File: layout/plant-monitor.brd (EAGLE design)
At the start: 42.2 x 23.8 mm, 11 parts, among them J1 AVR_SPI_PRG_6PTH

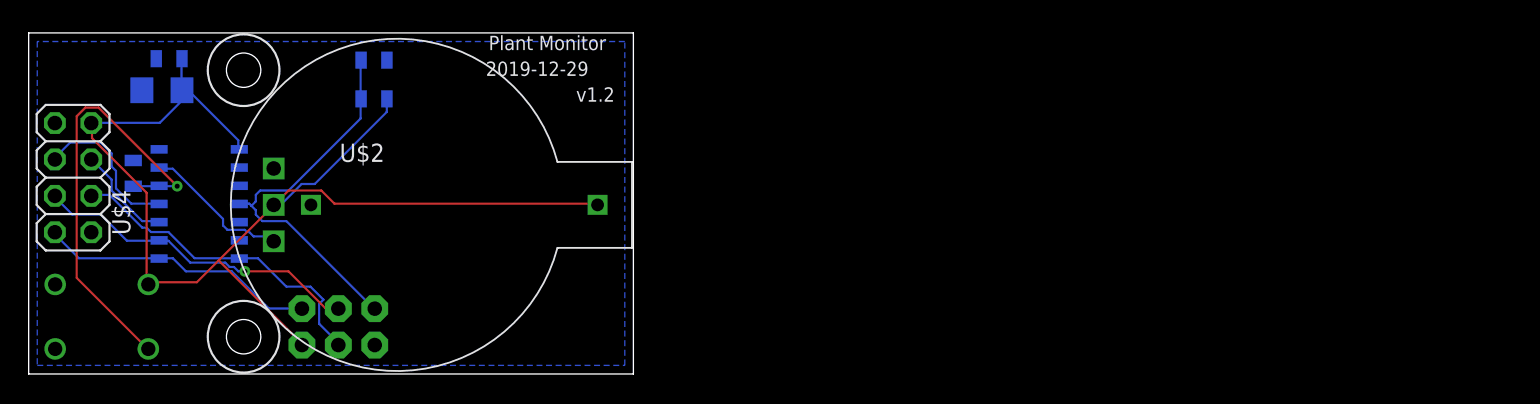
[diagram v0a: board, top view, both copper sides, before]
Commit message: Updated design to address problems in v1.3 board, notably ower switching added for soil sensor
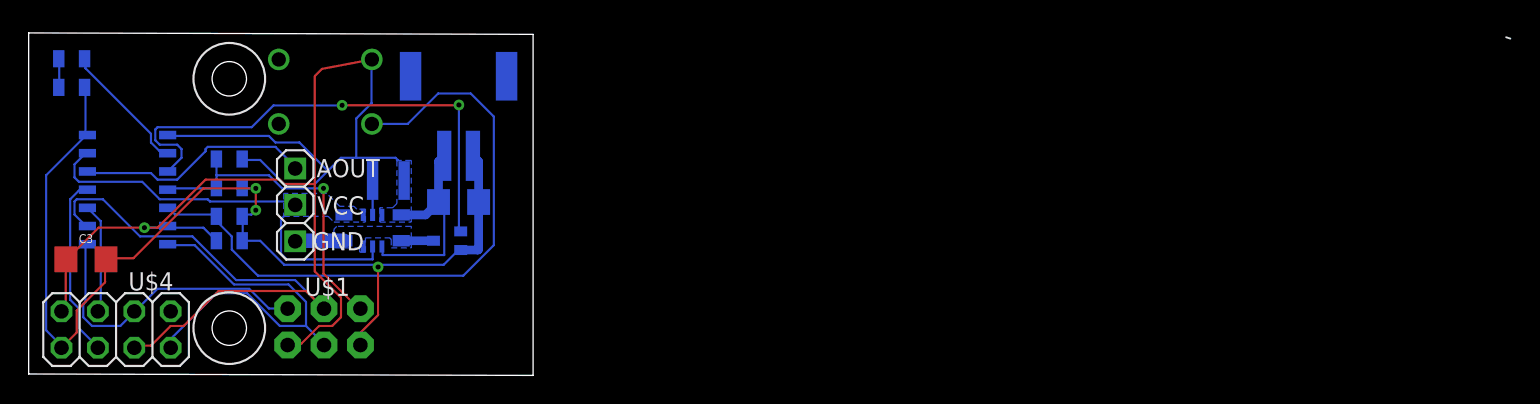
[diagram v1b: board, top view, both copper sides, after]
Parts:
- added C3: 10uF, SparkFun-Capacitors:1206
- added C5, C6: 10u, SparkFun:0805
- added R2: 300, SparkFun:0805
- added U$5: TPS6122X, GARTH:SC70-6
- added U$6: LED, GARTH:0805
- added U$8: BATT, GARTH:JST-PH-2
- added U$9: DMN53D0LW, GARTH:SOT-323
- U$1: value CAP-SOIL-SENSORRA -> CAP-SOIL-SENSOR; device GARTH:CAP-SOIL-SENSOR-RA -> GARTH:CAP-SOIL-SENSOR
- U$2: value 20MM-COIN-BATT -> 4.7u; device GARTH:20MM-COIN-BATT -> GARTH:LQH3NPN
- moved U$7 22.1 mm to (20.7, 19.7)
- moved C1 22.1 mm to (30.0, 12.0), turned to 180 degrees
- moved C4 13.5 mm to (14.0, 13.0)
- moved C2 13.4 mm to (14.0, 9.30), turned to 180 degrees
- moved U$4 11.0 mm to (6.10, 3.10), turned to 180 degrees
- moved R8 10.9 mm to (14.0, 15.0)
- moved R1 7.34 mm to (14.0, 11.0), turned to 0 degrees
- moved U$2 5.66 mm to (25.1, 13.5), flipped to the bottom
- moved U$3 5.10 mm to (6.90, 13.5)
- moved U$1 1.50 mm to (18.6, 11.8), flipped to the top, turned to 90 degrees
- moved J1 1.00 mm to (18.1, 4.56)
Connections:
- removed net MISO-DO: J1.1, U$3.8, U$4.MISO
- removed net MOSI-DI: J1.4, U$3.7, U$4.MOSI
- new net DI/(SPI-MOSI): J1.4, U$3.7, U$4.MISO
- new net DO/(SPI-MISO): J1.1, U$3.8, U$4.MOSI
- new net INDICATOR: R2.2, U$3.2
- new net N$1: R2.1, U$6.P$1
- new net N$2: U$2.P$2, U$5.P$5
- new net N$5: C5.2, C6.2, U$1.GND, U$5.P$3, U$9.P$1
- new net SENSOR_EN: U$3.3, U$9.P$2
- new net V5: C5.1, U$1.VCC, U$3.13, U$5.P$2, U$5.P$4
- net GND: now also C3.2, U$6.P$2, U$8.P$2, U$9.P$3; no longer U$1.GND, U$2.V-
- net SENSOR: now also U$3.12; no longer U$3.13
- net SETUP: now also U$3.5; no longer U$3.12
- net VCC: now also C3.1, C6.1, U$2.P$1, U$3.6, U$5.P$1, U$5.P$6, U$8.P$1; no longer U$1.VCC, U$2.V+
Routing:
- net GND: track 0.00 -> 75.7 mm, vias 0 -> 3
- net SENSOR_EN: track 0.00 -> 35.6 mm, vias 0 -> 2
- net V5: track 0.00 -> 28.7 mm
- net DI/(SPI-MOSI): track 0.00 -> 27.2 mm
- net MOSI-DI: track 23.1 -> 0.00 mm
- net DO/(SPI-MISO): track 0.00 -> 21.4 mm
- net MISO-DO: track 19.5 -> 0.00 mm
- net VCC: track 83.2 -> 102.7 mm, vias 0 -> 1
- net SCLK: track 23.1 -> 38.2 mm, vias 1 -> 0
- net SETUP: track 30.9 -> 45.3 mm, vias 1 -> 0
- net INDICATOR: track 0.00 -> 9.26 mm
- net SENSOR: track 10.4 -> 16.5 mm
- net N$5: track 0.00 -> 5.67 mm
- net SPI_RESET: track 27.2 -> 22.8 mm, vias 0 -> 1
- net N$2: track 0.00 -> 2.40 mm
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- added copper zone on layer 16, net N$5
- added copper zone on layer 16, net V5
- added copper zone on layer 16, net VCC
- removed copper zone on layer 16, net GND
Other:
- board size 42.2 x 23.8 mm -> 35.2 x 23.9 mm
- board text added: "2019-05-02"
- board text added: "v1.4"
- board text removed: "2019-12-29"
- board text removed: "v1.2"

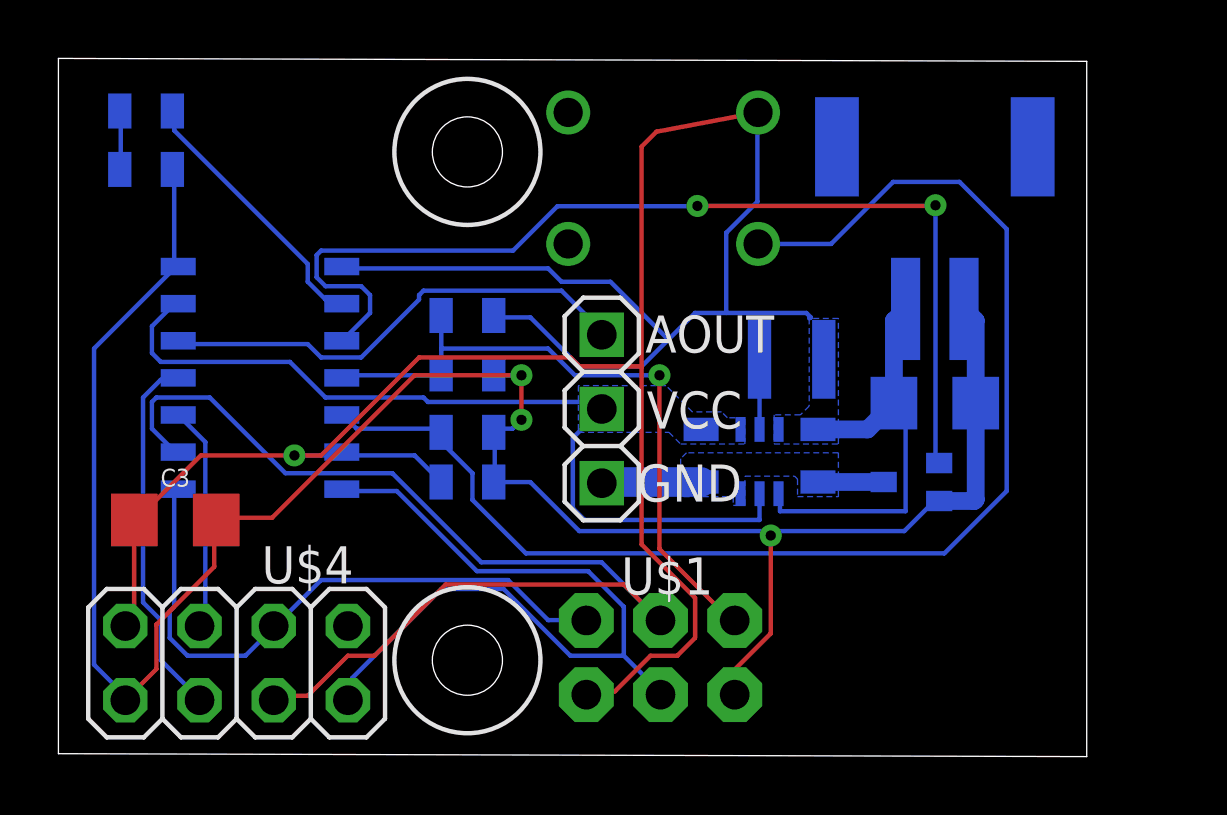
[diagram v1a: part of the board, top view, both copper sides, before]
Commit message: Updated board design that removes the voltage regulator.  The moisture meter does this and its not necessary
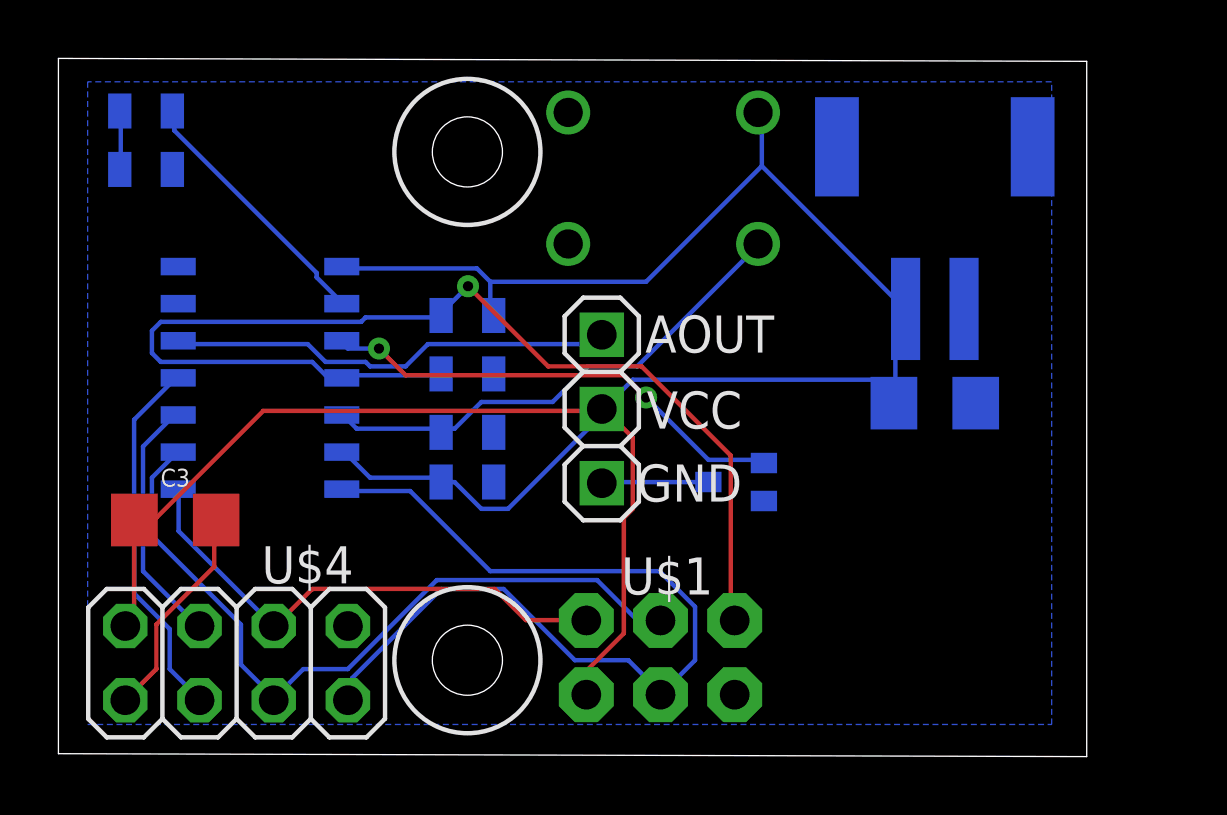
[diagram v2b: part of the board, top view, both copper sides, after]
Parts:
- removed C5, C6: 10u, SparkFun:0805
- removed U$2: 4.7u, GARTH:LQH3NPN
- removed U$5: TPS6122X, GARTH:SC70-6
- moved U$9 6.00 mm to (23.2, 9.30)
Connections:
- removed net N$2: U$2.P$2, U$5.P$5
- removed net V5: C5.1, U$1.VCC, U$3.13, U$5.P$2, U$5.P$4
- net N$5: no longer C5.2, C6.2, U$5.P$3
- net VCC: now also U$1.VCC; no longer C6.1, U$2.P$1, U$5.P$1, U$5.P$6
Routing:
- net GND: track 75.7 -> 7.45 mm, vias 3 -> 0
- net V5: track 28.7 -> 0.00 mm
- net SETUP: track 45.3 -> 17.3 mm
- net SENSOR_EN: track 35.6 -> 16.2 mm
- net VCC: track 102.7 -> 84.7 mm, vias 1 -> 0
- net SPI_RESET: track 22.8 -> 39.7 mm
- net SCLK: track 38.2 -> 26.1 mm
- net DI/(SPI-MOSI): track 27.2 -> 31.4 mm
- net DO/(SPI-MISO): track 21.4 -> 17.7 mm
- net N$2: track 2.40 -> 0.00 mm
- net N$5: track 5.67 -> 3.65 mm
- net SENSOR: track 16.5 -> 15.4 mm
- net RADIO_CSN: track 7.69 -> 8.62 mm
- added copper zone on layer 16, net GND
- removed copper zone on layer 16, net N$5
- removed copper zone on layer 16, net V5
- removed copper zone on layer 16, net VCC
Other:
- board text added: "2020-07-04"
- board text added: "v1.5"
- board text removed: "2019-05-02"
- board text removed: "v1.4"
